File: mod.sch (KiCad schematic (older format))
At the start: 29 parts

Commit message: modified:   mod-cache.lib 	modified:   mod.bak 	new file:   mod.mod 	renamed:    mod.bak -> mod.sch 	new file:   modsimple.brd 	new file:   modsimple.net 	new file:   modsimple.pro 	new file:   modsimple.sch
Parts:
- removed BT?: BATTERY, symbol BATTERY
- removed SW?: SW_PUSH, symbol SW_PUSH
- added Q2: FDD8870, symbol MOSFET_N
- added R?: 10K, symbol R
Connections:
- net labels added: Atomizer (+), Atomizer (-), Battery (+), Battery (-), Switch (+), Switch (-)
- wire segments 93 -> 102
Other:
- note added: "For the ISL97656 Boost converter:\nVout=1.24*(1+R1/R2)\nFor Two resisters use ranges between 22K-55K for R1 & R2=10K\nOR use MCP4013 (digital potentiometer with the B terminal interally wired to ground resulting in a voltage divider circuit.)\n"
- note removed: "Vout=1.24*(1+R1/R2)\nFor Two resisters use ranges between 22K-55K for R1 & R2=10K"
- moved on the sheet: J?, P?

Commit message: Added two sided board
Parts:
- removed U?: MCP4013, symbol MCP4013
- added R?: 10K, symbol R
- added R?: 39k, symbol R
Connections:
- wire segments 102 -> 92

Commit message: part selection changes (again)
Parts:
- removed C1: 27nF, symbol C
- removed C2, C3: 22uF, symbol C
- removed C4: 0.1uF, symbol C
- removed C5: 4.7nF, symbol C
- removed D1: DIODESCH, symbol DIODESCH
- removed D? (x2): LED, symbol LED
- removed IC?: ATTINY45-S, SO8-200, symbol ATTINY45-S
- removed IC?: ATMEGA168A-A, TQFP32, symbol ATMEGA168A-A
- removed JP? (x2): JUMPER3, symbol JUMPER3
- removed L?: 10uH, symbol INDUCTOR
- removed Q?: PN2222A, TO92, symbol PN2222A
- removed R5, R?: 10K, symbol R
- removed R6: 1K, symbol R
- removed R?: R, symbol R
- removed R?: 39k, symbol R
- removed U?: MAX1555, symbol MAX1555
- removed U?: ISL97656, symbol ISL97656
- added C? (x2): CP1, symbol CP1
- added C? (x4): 4.7uF, symbol C
- added D?: DIODESCH, symbol DIODESCH
- added L?: INDUCTOR, symbol INDUCTOR
- added Q?: FDD8870, symbol MOSFET_N
- added R? (x4): 2K, symbol R
- added U1: MCP73831, ~, symbol MCP73831
- added U?: LTC1871, ~, symbol LTC1871
- C1, C2: renamed from C?; value 1uF -> 4.7uF
- R3: value 3.9K -> 330
- R4: value 2k2 -> 2K
- gave numbers to parts that had none: 4
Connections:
- net labels added: Atomizer+, Atomizer-, Battery+, Battery-, FireLED+, FireLED-, Switch+, Switch-, chgLED+, chgLED-
- net labels removed: Atomizer (+), Atomizer (-), Battery (+), Battery (-), Switch (+), Switch (-)
- wire segments 92 -> 84
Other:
- note added: "Values Not yet Set for boost converter"
- note added: "x2?"
- note added: "x4?"
- note removed: "For the ISL97656 Boost converter:\nVout=1.24*(1+R1/R2)\nFor Two resisters use ranges between 22K-55K for R1 & R2=10K\nOR use MCP4013 (digital potentiometer with the B terminal interally wired to ground resulting in a voltage divider circuit.)\n"
- moved on the sheet: C1, C2, Q2, R1, R2

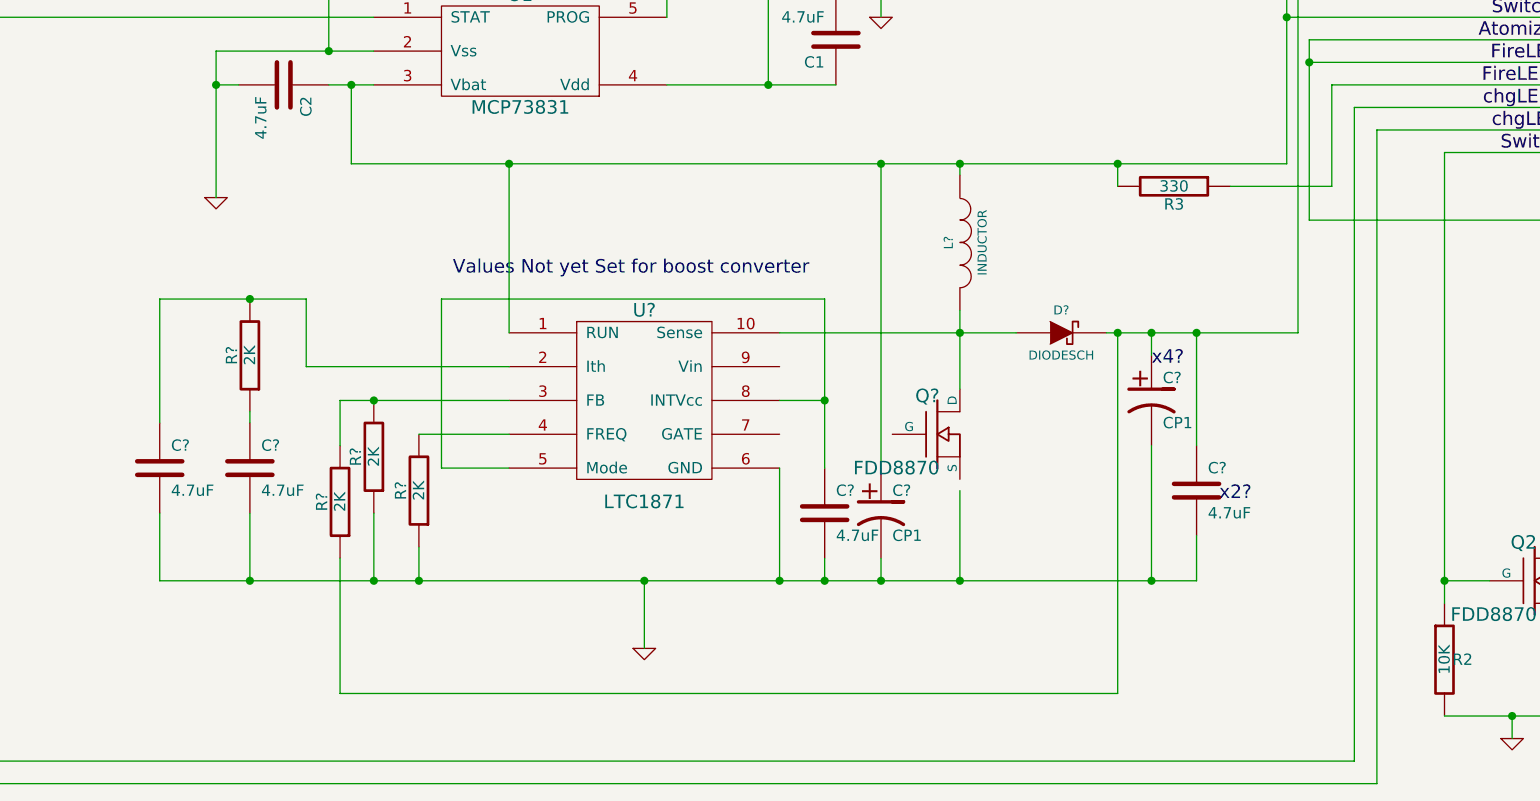
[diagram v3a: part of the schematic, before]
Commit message: finished boost schematic
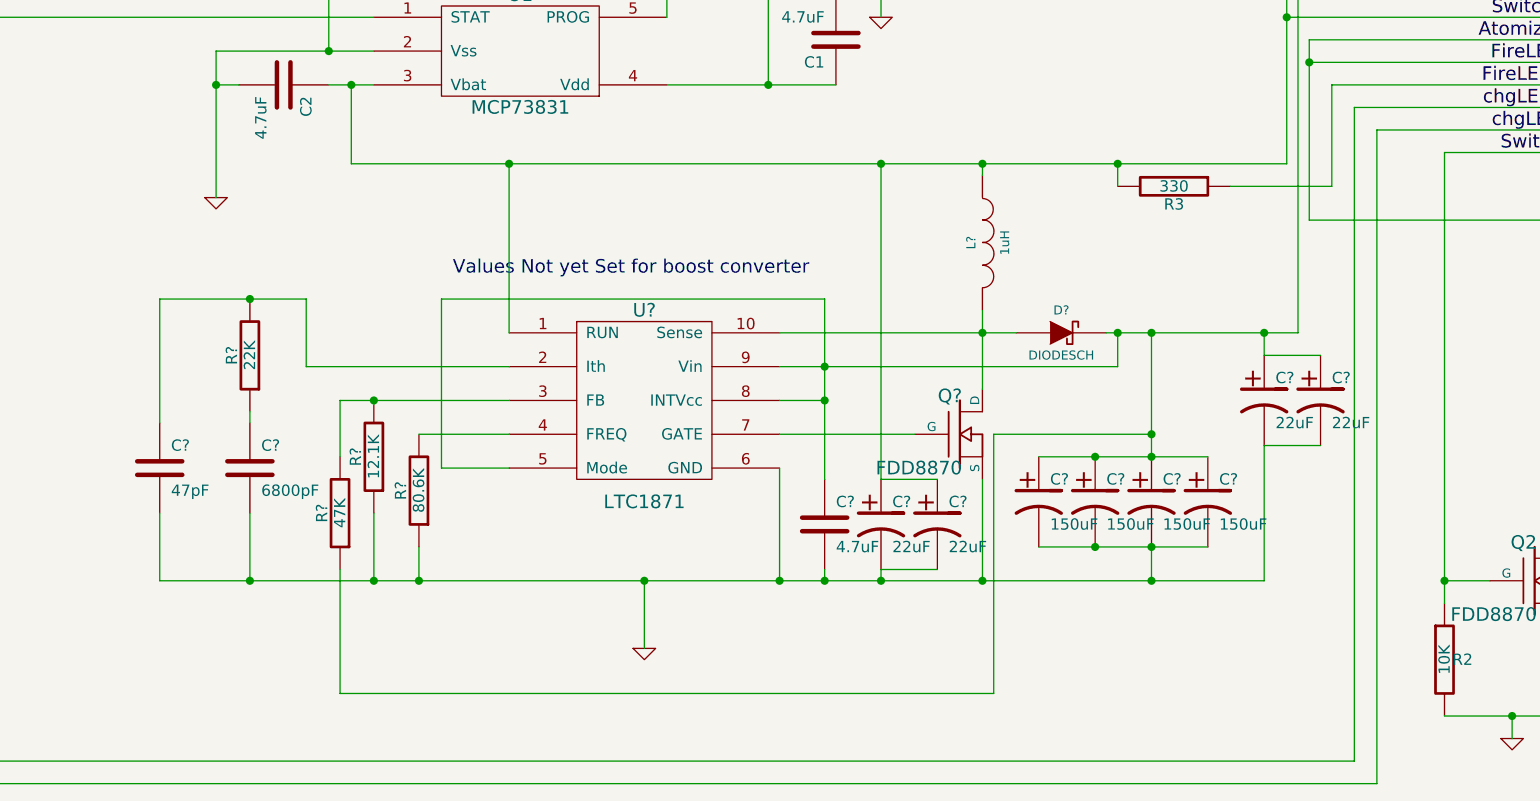
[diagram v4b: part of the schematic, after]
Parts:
- removed C?: 4.7uF, symbol C
- added C? (x3): 22uF, symbol CP1
- added C? (x3): 150uF, symbol CP1
- C?: value CP1 -> 22uF
- C?: value CP1 -> 150uF
- C?: value 4.7uF -> 47pF
- C?: value 4.7uF -> 6800pF
- L?: value INDUCTOR -> 1uH
- R?: value 2K -> 22K
- R?: value 2K -> 47K
- R?: value 2K -> 12.1K
- R?: value 2K -> 80.6K
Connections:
- net Atomizer+: now also C?.1, U?.5 (Mode), U?.8 (INTVcc), U?.9 (Vin), C?.1, C?.1, C?.1, C?.1, C?.1
- net Battery+: now also C?.1
- net GND: now also Q?.S, C?.2, C?.2, C?.2, C?.2, C?.2, C?.2
- net at U?.7 (GATE): now also Q?.G
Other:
- note removed: "x2?"
- note removed: "x4?"
- moved on the sheet: C?, L?, Q?, R?

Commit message: progress on booster circuit
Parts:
- removed C1, C2, C?: 4.7uF, symbol C
- removed C? (x4): 22uF, symbol CP1
- removed C? (x4): 150uF, symbol CP1
- removed C?: 47pF, symbol C
- removed C?: 6800pF, symbol C
- removed D?: DIODESCH, symbol DIODESCH
- removed L?: 1uH, symbol INDUCTOR
- removed P1: CONN_10, symbol CONN_10
- removed Q?: FDD8870, symbol MOSFET_N
- removed R1: 330, symbol R
- removed R4: 2K, symbol R
- removed R?: 22K, symbol R
- removed R?: 47K, symbol R
- removed R?: 12.1K, symbol R
- removed R?: 80.6K, symbol R
- removed U1: MCP73831, ~, symbol MCP73831
- removed U?: LTC1871, ~, symbol LTC1871
- added IC1: ATTINY85-S, SO8-200, symbol ATTINY85-S
- added P1: CONN_12, symbol CONN_12
- added R10, R11, R12, R5, R6, R7, R8, R9: 330, symbol R
- added SW1, SW2, SW3: SW_PUSH_SMALL, symbol SW_PUSH_SMALL
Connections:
- net Atomizer+: now also P1.3 (P3)
- net Atomizer-: now also P1.5 (P5), P1.6 (P6), R5.2, R6.1
- net Battery+: now also R3.1, IC1.8 (VCC), P1.2 (P2), R10.1, R11.1, R12.1, R8.2, R9.1; no longer R3.2
- net FireLED+: now also R3.2, P1.7 (P7); no longer R3.1
- net GND: now also R2.1, IC1.4 (GND), P1.1 (P1), P1.4 (P4), R5.1, R7.1, SW1.2, SW2.2, SW3.2; no longer R2.2
- net MCP73831 Charger/Vcharge: now reaches J1.1 (Vbus)
- net Switch-: no longer names the net of Q2.G
- net Switch-: now also R2.2, IC1.3 (PB4(XTAL2/CLKO/OC1B/ADC2/PCINT4)); no longer R2.1
- new net: IC1.5 (PB0(MOSI/DI/SDA/AIN0/OC0A/OC1A/AREF/PCINT0)), R7.2, R8.1
- new net: IC1.6 (PB1(MISO/DO/AIN1/OC0B/OC1A/PCINT1)), R6.2
- new net ChargeLED+: P1.8 (P8), R9.2
- new net ChargeLED-: P1.9 (P9)
- new net DWN-MCU: IC1.2 (PB3(XTAL1/CLKI/OC1B/ADC3/PCINT3)), P1.11 (P11), R11.2, SW2.1
- new net FIRE-MCU: IC1.1 (PB5(~RESET~/dW/ADC0/PCINT5)), P1.12 (P12), R12.2, SW3.1
- new net UP-MCU: IC1.7 (PB2(SCK/USCK/SCL/T0/INT0/ADC1/PCINT2)), P1.10 (P10), R10.2, SW1.1
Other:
- note added: "On-board buttons for testing/chassis mount"
- note added: "UP,DWN,&FIRE pullup values not set"
- note added: "Vdiv for Vatty feedback"
- note added: "Vdiv for Vbat monitoring"
- note removed: "Values Not yet Set for boost converter"
- moved on the sheet: R3

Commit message: progress on layout
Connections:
- net Atomizer-: no longer R5.2
- net UP-MCU: now also IC1.3 (PB4(XTAL2/CLKO/OC1B/ADC2/PCINT4)); no longer IC1.7 (PB2(SCK/USCK/SCL/T0/INT0/ADC1/PCINT2))
- net at Q2.G, R2.2: now also IC1.5 (PB0(MOSI/DI/SDA/AIN0/OC0A/OC1A/AREF/PCINT0)); no longer IC1.3 (PB4(XTAL2/CLKO/OC1B/ADC2/PCINT4))
- net at R7.2, R8.1: now also IC1.7 (PB2(SCK/USCK/SCL/T0/INT0/ADC1/PCINT2)); no longer IC1.5 (PB0(MOSI/DI/SDA/AIN0/OC0A/OC1A/AREF/PCINT0))
- net at IC1.6 (PB1(MISO/DO/AIN1/OC0B/OC1A/PCINT1)), R6.2: now also R5.2
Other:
- moved on the sheet: R5, R6, R7, R8
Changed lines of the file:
@@
-EESchema Schematic File Version 2  date Fri 29 Mar 2013 12:02:52 PM CDT
+EESchema Schematic File Version 2  date Fri 29 Mar 2013 11:41:29 PM CDT
 LIBS:power
 LIBS:device
@@
 Sheet 1 3
 Title ""
-Date "29 mar 2013"
+Date "30 mar 2013"
 Rev ""
 Comp ""
@@
 Atomizer-
 $Comp
-L GND #PWR3
+L GND #PWR01
 U 1 1 51302ACE
 P 9800 6500
-F 0 "#PWR3" H 9800 6500 30  0001 C CNN
+F 0 "#PWR01" H 9800 6500 30  0001 C CNN
 F 1 "GND" H 9800 6430 30  0001 C CNN
 F 2 "" H 9800 6500 60  0001 C CNN
@@
 Battery+
 $Comp
-L GND #PWR5
+L GND #PWR02
 U 1 1 512C4AF2
 P 11200 3800
-F 0 "#PWR5" H 11200 3800 30  0001 C CNN
+F 0 "#PWR02" H 11200 3800 30  0001 C CNN
 F 1 "GND" H 11200 3730 30  0001 C CNN
 F 2 "" H 11200 3800 60  0001 C CNN
@@
 $EndComp
 $Comp
-L GND #PWR2
+L GND #PWR03
 U 1 1 512AF9E3
 P 9700 2550
-F 0 "#PWR2" H 9700 2550 30  0001 C CNN
+F 0 "#PWR03" H 9700 2550 30  0001 C CNN
 F 1 "GND" H 9700 2480 30  0001 C CNN
 F 2 "" H 9700 2550 60  0001 C CNN
@@
 $EndComp
 $Comp
-L GND #PWR1
+L GND #PWR04
 U 1 1 5155BA90
 P 5450 5450
-F 0 "#PWR1" H 5450 5450 30  0001 C CNN
+F 0 "#PWR04" H 5450 5450 30  0001 C CNN
 F 1 "GND" H 5450 5380 30  0001 C CNN
 F 2 "" H 5450 5450 60  0001 C CNN
@@
 L R R8
 U 1 1 5155BB33
-P 4600 4050
-F 0 "R8" V 4680 4050 50  0000 C CNN
-F 1 "330" V 4600 4050 50  0000 C CNN
-F 2 "" H 4600 4050 60  0001 C CNN
-F 3 "" H 4600 4050 60  0001 C CNN
-	1    4600 4050
+P 4250 4100
+F 0 "R8" V 4330 4100 50  0000 C CNN
+F 1 "330" V 4250 4100 50  0000 C CNN
+F 2 "" H 4250 4100 60  0001 C CNN
+F 3 "" H 4250 4100 60  0001 C CNN
+	1    4250 4100
 	-1   0    0    1
 $EndComp
@@
 L R R7
 U 1 1 5155BB45
-P 4300 4350
-F 0 "R7" V 4380 4350 50  0000 C CNN
-F 1 "330" V 4300 4350 50  0000 C CNN
-F 2 "" H 4300 4350 60  0001 C CNN
-F 3 "" H 4300 4350 60  0001 C CNN
-	1    4300 4350
-	0    -1   -1   0
-$EndComp
-Text Notes 4750 4050 0    60   ~ 0
+P 3900 4650
+F 0 "R7" V 3980 4650 50  0000 C CNN
+F 1 "330" V 3900 4650 50  0000 C CNN
+F 2 "" H 3900 4650 60  0001 C CNN
+F 3 "" H 3900 4650 60  0001 C CNN
+	1    3900 4650
+	0    -1   -1   0
+$EndComp
+Text Notes 4750 4350 0    60   ~ 0
 Vdiv for Vbat monitoring
 $Comp
 L R R6
 U 1 1 5155BC78
-P 3600 4550
-F 0 "R6" V 3680 4550 50  0000 C CNN
-F 1 "330" V 3600 4550 50  0000 C CNN
-F 2 "" H 3600 4550 60  0001 C CNN
-F 3 "" H 3600 4550 60  0001 C CNN
-	1    3600 4550
+P 3100 4550
+F 0 "R6" V 3180 4550 50  0000 C CNN
+F 1 "330" V 3100 4550 50  0000 C CNN
+F 2 "" H 3100 4550 60  0001 C CNN
+F 3 "" H 3100 4550 60  0001 C CNN
+	1    3100 4550
 	0    -1   -1   0
 $EndComp
@@
 L R R5
 U 1 1 5155C2FA
-P 3350 4900
-F 0 "R5" V 3430 4900 50  0000 C CNN
-F 1 "330" V 3350 4900 50  0000 C CNN
-F 2 "" H 3350 4900 60  0001 C CNN
-F 3 "" H 3350 4900 60  0001 C CNN
-	1    3350 4900
+P 3400 4900
+F 0 "R5" V 3480 4900 50  0000 C CNN
+F 1 "330" V 3400 4900 50  0000 C CNN
+F 2 "" H 3400 4900 60  0001 C CNN
+F 3 "" H 3400 4900 60  0001 C CNN
+	1    3400 4900
 	-1   0    0    1
 $EndComp
@@
 	10050 2450 10050 3000
 Wire Wire Line
-	4600 3100 10050 3100
+	4250 3100 8050 3100
+Wire Wire Line
+	8050 3100 10050 3100
 Wire Wire Line
 	11100 3600 11200 3600
@@
 	11200 3600 11200 3800
 Wire Wire Line
-	8900 3400 8900 5400
-Wire Wire Line
-	8900 5400 10300 5400
+	8900 3400 8900 3500
+Wire Wire Line
+	8900 3500 8900 5400
+Wire Wire Line
+	8900 5400 10000 5400
+Wire Wire Line
+	10000 5400 10300 5400
 Wire Wire Line
 	10000 5400 10000 5600
@@
 	10000 6400 10000 6000
 Wire Wire Line
-	9500 6400 10000 6400
+	9500 6400 9800 6400
+Wire Wire Line
+	9800 6400 10000 6400
 Wire Wire Line
 	9800 6400 9800 6500
@@
 Connection ~ 8050 3100
 Wire Wire Line
-	9700 2450 10350 2450
+	9700 2450 10050 2450
+Wire Wire Line
+	10050 2450 10350 2450
 Wire Wire Line
 	9700 2450 9700 2550
@@
 	5450 5300 5450 5450
 Wire Wire Line
-	3350 5300 8050 5300
+	3400 5300 3600 5300
+Wire Wire Line
+	3600 5300 5450 5300
+Wire Wire Line
+	5450 5300 8050 5300
 Connection ~ 5450 5300
 Wire Wire Line
-	4600 3800 4600 3100
-Wire Wire Line
-	3000 6700 10300 6700
+	4250 3850 4250 3100
+Wire Wire Line
+	2850 6700 10300 6700
 Wire Wire Line
 	10300 6700 10300 5400
@@
 	8050 4950 7650 4950
 Wire Wire Line
-	4600 4450 4950 4450
-Wire Wire Line
-	4600 4300 4600 4450
-Wire Wire Line
-	3000 4550 3000 6700
-Wire Wire Line
-	4950 4550 3850 4550
-Wire Wire Line
-	3350 4550 3350 4650
-Wire Wire Line
-	3000 4550 3350 4550
-Wire Wire Line
-	3350 5150 3350 5300
-Wire Wire Line
-	4600 5800 9700 5800
-Wire Wire Line
-	4600 5800 4600 4850
-Wire Wire Line
-	4600 4850 4950 4850
+	4250 4350 4250 4650
+Wire Wire Line
+	2850 4550 2850 6700
+Wire Wire Line
+	3350 4550 3400 4550
+Wire Wire Line
+	3400 4550 4950 4550
+Wire Wire Line
+	3400 5150 3400 5300
+Wire Wire Line
+	4800 5800 9500 5800
+Wire Wire Line
+	9500 5800 9700 5800
 Wire Wire Line
 	9500 5900 9500 5800
@@
 Connection ~ 10050 2450
 Wire Wire Line
-	4550 4350 4600 4350
-Connection ~ 4600 4350
-Wire Wire Line
-	8650 4100 10050 4100
-Wire Wire Line
-	4050 4350 3950 4350
-Wire Wire Line
-	3950 4350 3950 5300
-Connection ~ 3950 5300
+	4150 4650 4250 4650
+Wire Wire Line
+	4250 4650 4950 4650
+Connection ~ 4250 4650
+Wire Wire Line
+	8650 4100 10000 4100
+Wire Wire Line
+	10000 4100 10050 4100
+Wire Wire Line
+	3650 4650 3600 4650
+Wire Wire Line
+	3600 4650 3600 5300
+Connection ~ 3600 5300
 Wire Wire Line
 	8050 4100 8150 4100
@@
 Connection ~ 8050 4100
 Wire Wire Line
-	8650 4000 10050 4000
-Wire Wire Line
-	8650 3900 10050 3900
-Wire Wire Line
-	8050 1250 8050 4450
+	8650 4000 9950 4000
+Wire Wire Line
+	9950 4000 10050 4000
+Wire Wire Line
+	8650 3900 9850 3900
+Wire Wire Line
+	9850 3900 10050 3900
+Wire Wire Line
+	8050 1250 8050 1750
+Wire Wire Line
+	8050 1750 8050 3100
+Wire Wire Line
+	8050 3100 8050 3600
+Wire Wire Line
+	8050 3600 8050 3700
+Wire Wire Line
+	8050 3700 8050 3900
+Wire Wire Line
+	8050 3900 8050 4000
+Wire Wire Line
+	8050 4000 8050 4100
+Wire Wire Line
+	8050 4100 8050 4450
 Wire Wire Line
 	8150 3600 8050 3600
 Connection ~ 8050 3600
 Wire Wire Line
-	4950 4650 4300 4650
+	4950 4850 4300 4850
 Wire Wire Line
 	4950 4750 4300 4750
@@
 	9850 4500 9850 3900
 Connection ~ 9850 3900
-Text Label 4300 4650 0    60   ~ 0
+Text Label 4300 4850 0    60   ~ 0
 UP-MCU
 Text Label 4300 4750 0    60   ~ 0
@@
 $EndComp
 $Comp
-L GND #PWR4
+L GND #PWR05
 U 1 1 5155E12D
 P 10600 4850
-F 0 "#PWR4" H 10600 4850 30  0001 C CNN
+F 0 "#PWR05" H 10600 4850 30  0001 C CNN
 F 1 "GND" H 10600 4780 30  0001 C CNN
 F 2 "" H 10600 4850 60  0001 C CNN
@@
 $EndComp
 Wire Wire Line
-	10600 4600 10600 4850
+	10600 4600 10600 4800
+Wire Wire Line
+	10600 4800 10600 4850
 Wire Wire Line
 	10300 4700 10300 4800
 Wire Wire Line
-	10300 4800 10950 4800
+	10300 4800 10600 4800
+Wire Wire Line
+	10600 4800 10950 4800
 Connection ~ 10600 4800
 Wire Wire Line
@@
 Text Label 1900 1400 2    60   ~ 0
 ChargeLED-
+Wire Wire Line
+	3400 4650 3400 4550
+Connection ~ 3400 4550
+Wire Wire Line
+	4800 5800 4800 4450
+Wire Wire Line
+	4800 4450 4950 4450
 $EndSCHEMATC

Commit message: many changes. Most not stable. Check TODO
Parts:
- removed R3: 330, symbol R
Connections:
- net Atomizer-: no longer P1.6 (P6)
- net FIRE-MCU: now also IC1.3 (PB4(XTAL2/CLKO/OC1B/ADC2/PCINT4)); no longer IC1.1 (PB5(~RESET~/dW/ADC0/PCINT5))
- net UP-MCU: now also IC1.1 (PB5(~RESET~/dW/ADC0/PCINT5)); no longer IC1.3 (PB4(XTAL2/CLKO/OC1B/ADC2/PCINT4))
- net FireLED+: no longer names the net of P1.7 (P7)
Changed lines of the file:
@@
-EESchema Schematic File Version 2  date Fri 29 Mar 2013 11:41:29 PM CDT
+EESchema Schematic File Version 2  date Sat 30 Mar 2013 02:51:58 PM CDT
 LIBS:power
 LIBS:device
@@
 $EndDescr
 $Comp
-L R R3
-U 1 1 5133879A
-P 8400 3600
-F 0 "R3" V 8480 3600 50  0000 C CNN
-F 1 "330" V 8400 3600 50  0000 C CNN
-F 2 "" H 8400 3600 60  0001 C CNN
-F 3 "" H 8400 3600 60  0001 C CNN
-	1    8400 3600
-	0    -1   -1   0
-$EndComp
-$Comp
 L R R2
 U 1 1 5131879B
@@
 	1    0    0    -1
 $EndComp
-Text Label 10050 3600 2    60   ~ 0
-FireLED+
-Text Label 10050 3500 2    60   ~ 0
-FireLED-
 $Sheet
 S 550  1000 700  500
@@
 	10050 2450 10050 3000
 Wire Wire Line
-	4250 3100 8050 3100
-Wire Wire Line
-	8050 3100 10050 3100
+	4250 3100 10050 3100
 Wire Wire Line
 	11100 3600 11200 3600
@@
 	11200 3600 11200 3800
 Wire Wire Line
-	8900 3400 8900 3500
-Wire Wire Line
-	8900 3500 8900 5400
-Wire Wire Line
-	8900 5400 10000 5400
-Wire Wire Line
-	10000 5400 10300 5400
+	8900 3400 8900 5400
+Wire Wire Line
+	8900 5400 10300 5400
 Wire Wire Line
 	10000 5400 10000 5600
 Wire Wire Line
-	8650 3600 10050 3600
-Wire Wire Line
 	8900 3400 10050 3400
-Wire Wire Line
-	8900 3500 10050 3500
-Connection ~ 8900 3500
 Connection ~ 6500 550
 Wire Wire Line
 	10000 6400 10000 6000
 Wire Wire Line
-	9500 6400 9800 6400
-Wire Wire Line
-	9800 6400 10000 6400
+	9500 6400 10000 6400
 Wire Wire Line
 	9800 6400 9800 6500
@@
 Connection ~ 8050 3100
 Wire Wire Line
-	9700 2450 10050 2450
-Wire Wire Line
-	10050 2450 10350 2450
+	9700 2450 10350 2450
 Wire Wire Line
 	9700 2450 9700 2550
@@
 	5450 5300 5450 5450
 Wire Wire Line
-	3400 5300 3600 5300
-Wire Wire Line
-	3600 5300 5450 5300
-Wire Wire Line
-	5450 5300 8050 5300
+	3400 5300 8050 5300
 Connection ~ 5450 5300
 Wire Wire Line
@@
 	2850 4550 2850 6700
 Wire Wire Line
-	3350 4550 3400 4550
-Wire Wire Line
-	3400 4550 4950 4550
+	3350 4550 4950 4550
 Wire Wire Line
 	3400 5150 3400 5300
 Wire Wire Line
-	4800 5800 9500 5800
-Wire Wire Line
-	9500 5800 9700 5800
+	4800 5800 9700 5800
 Wire Wire Line
 	9500 5900 9500 5800
@@
 Connection ~ 10050 2450
 Wire Wire Line
-	4150 4650 4250 4650
-Wire Wire Line
-	4250 4650 4950 4650
+	4150 4650 4950 4650
 Connection ~ 4250 4650
 Wire Wire Line
-	8650 4100 10000 4100
-Wire Wire Line
-	10000 4100 10050 4100
+	8650 4100 10050 4100
 Wire Wire Line
 	3650 4650 3600 4650
@@
 Connection ~ 8050 4100
 Wire Wire Line
-	8650 4000 9950 4000
-Wire Wire Line
-	9950 4000 10050 4000
-Wire Wire Line
-	8650 3900 9850 3900
-Wire Wire Line
-	9850 3900 10050 3900
-Wire Wire Line
-	8050 1250 8050 1750
-Wire Wire Line
-	8050 1750 8050 3100
-Wire Wire Line
-	8050 3100 8050 3600
-Wire Wire Line
-	8050 3600 8050 3700
-Wire Wire Line
-	8050 3700 8050 3900
-Wire Wire Line
-	8050 3900 8050 4000
-Wire Wire Line
-	8050 4000 8050 4100
-Wire Wire Line
-	8050 4100 8050 4450
-Wire Wire Line
-	8150 3600 8050 3600
-Connection ~ 8050 3600
+	8650 4000 10050 4000
+Wire Wire Line
+	8650 3900 10050 3900
+Wire Wire Line
+	8050 1250 8050 4450
+Wire Wire Line
+	4950 4950 4300 4950
+Wire Wire Line
+	4950 4750 4300 4750
 Wire Wire Line
 	4950 4850 4300 4850
-Wire Wire Line
-	4950 4750 4300 4750
-Wire Wire Line
-	4950 4950 4300 4950
 Wire Wire Line
 	10000 4300 10000 4100
@@
 	9850 4500 9850 3900
 Connection ~ 9850 3900
-Text Label 4300 4850 0    60   ~ 0
+Text Label 4300 4950 0    60   ~ 0
 UP-MCU
 Text Label 4300 4750 0    60   ~ 0
 DWN-MCU
-Text Label 4300 4950 0    60   ~ 0
+Text Label 4300 4850 0    60   ~ 0
 FIRE-MCU
 Wire Wire Line
@@
 $EndComp
 Wire Wire Line
-	10600 4600 10600 4800
-Wire Wire Line
-	10600 4800 10600 4850
+	10600 4600 10600 4850
 Wire Wire Line
 	10300 4700 10300 4800
 Wire Wire Line
-	10300 4800 10600 4800
-Wire Wire Line
-	10600 4800 10950 4800
+	10300 4800 10950 4800
 Connection ~ 10600 4800
 Wire Wire Line
